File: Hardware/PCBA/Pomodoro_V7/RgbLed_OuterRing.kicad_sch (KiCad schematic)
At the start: 34 parts, among them J2 Conn_01x01_Pin

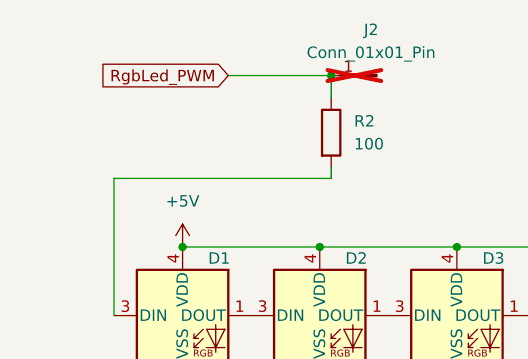
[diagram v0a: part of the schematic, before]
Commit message: Verified the microcontroller Pinout; Added basic peripheral wiring; Added the USBC Wiring
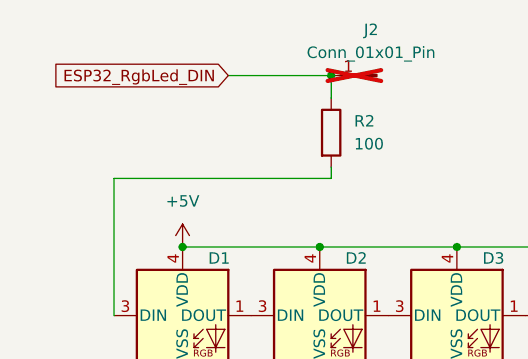
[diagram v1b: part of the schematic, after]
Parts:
- J2: now left out of the parts list
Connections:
- net RgbLed_PWM renamed ESP32_RgbLed_DIN
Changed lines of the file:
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@@
 		)
 	)
-	(global_label "RgbLed_PWM"
+	(global_label "ESP32_RgbLed_DIN"
 		(shape input)
 		(at 48.26 19.05 180)
@@
 		)
 		(property "Intersheetrefs" "${INTERSHEET_REFS}"
-			(at 33.3007 19.05 0)
+			(at 27.2531 19.05 0)
 			(effects
 				(font
@@
 		(unit 1)
 		(exclude_from_sim no)
-		(in_bom yes)
+		(in_bom no)
 		(on_board yes)
 		(dnp yes)

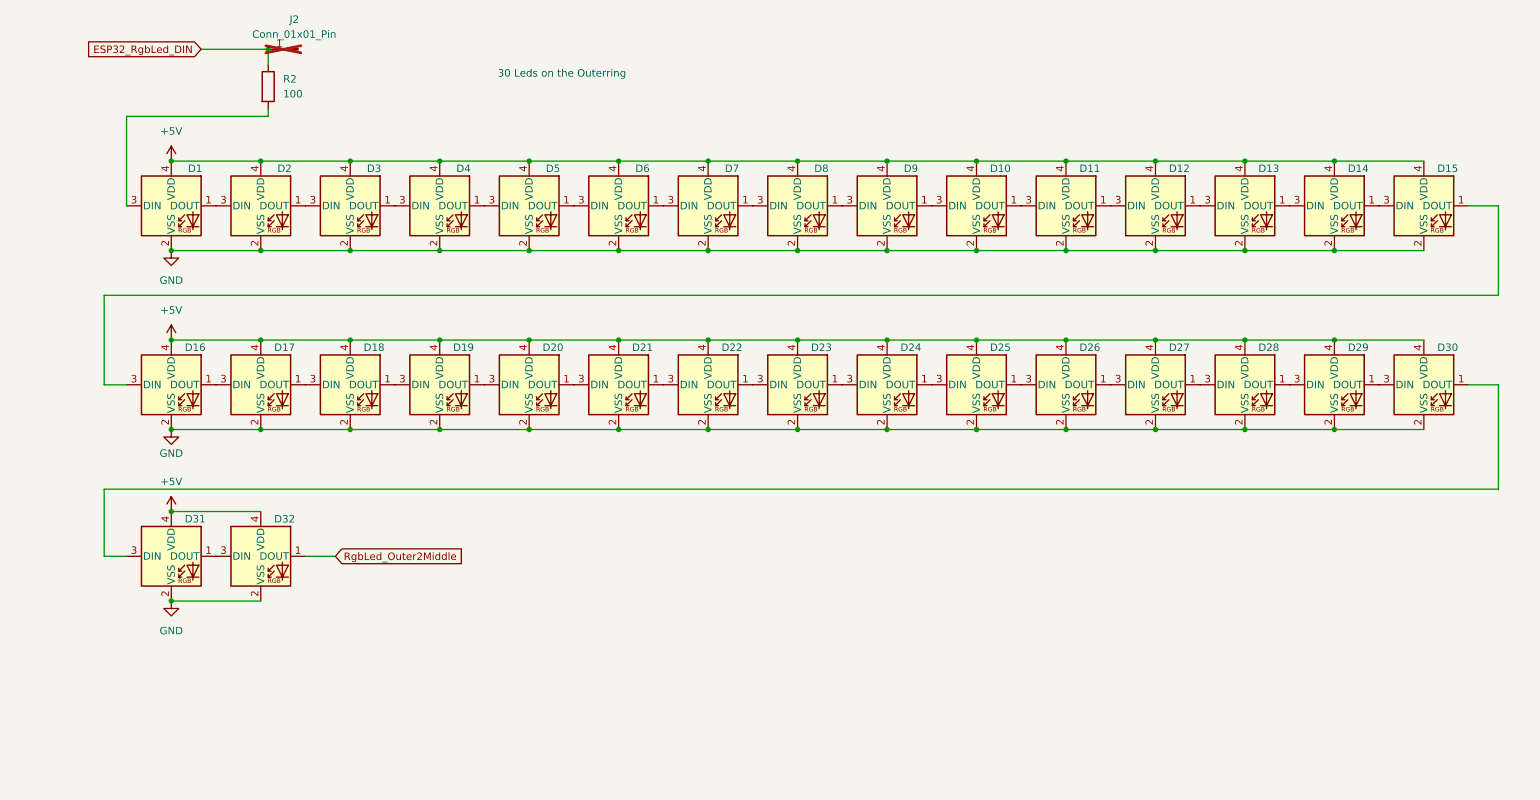
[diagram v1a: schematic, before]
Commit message: FW can now be flashed to an ESP32-S2 Target; Completed the Schematic
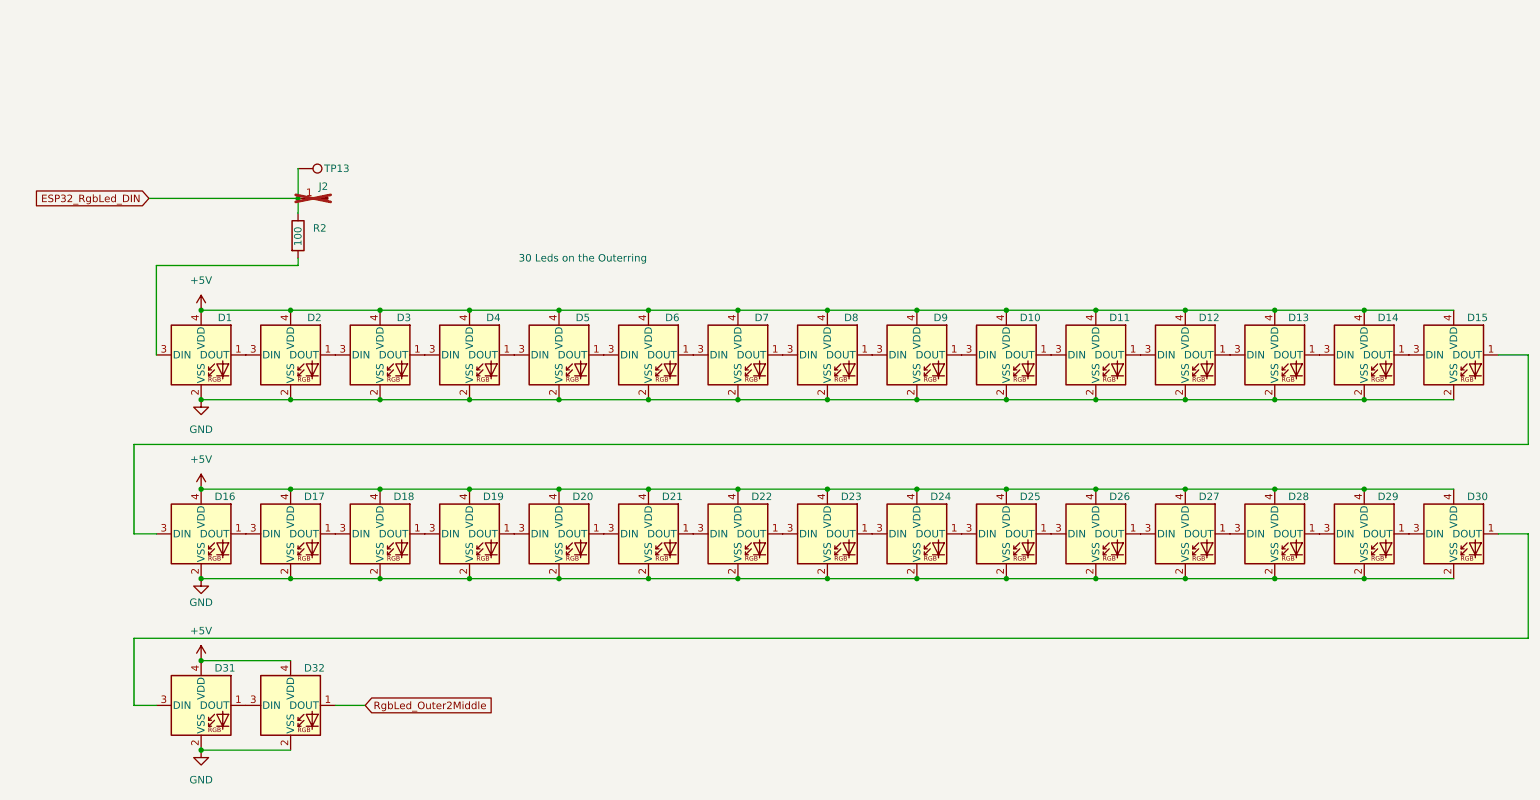
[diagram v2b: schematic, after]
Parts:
- added TP13: TestPoint, TestPoint:TestPoint_Pad_D1.0mm, symbol Connector:TestPoint
- J2: now in the parts list
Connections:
- net ESP32_RgbLed_DIN: now also TP13.1
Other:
- moved on the sheet: D1, D10, D11, D12, D13, D14, D15, D16, D17, D18, D19, D2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

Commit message: Update on the PCBA
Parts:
- renumbered J2 to J14, R2 to R11, TP13 to TP34
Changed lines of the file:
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@@
 		(dnp no)
 		(fields_autoplaced yes)
-		(property "Reference" "#PWR011"
+		(property "Reference" "#PWR051"
 			(at 48.26 97.79 0)
 			(effects
@@
 			(project "Pomodoro_V7"
 				(path "/7b50fc13-bee1-48b7-8eab-d6ef36855383/d366a572-4eed-4be8-88cc-5fb5da022e23/b6c0abfc-b228-4088-82f2-4b654b638967"
-					(reference "#PWR011")
+					(reference "#PWR051")
 					(unit 1)
 				)
@@
 		(on_board yes)
 		(dnp no)
-		(property "Reference" "R2"
+		(property "Reference" "R11"
 			(at 67.31 49.5299 0)
 			(effects
@@
 			(project "Pomodoro_V7"
 				(path "/7b50fc13-bee1-48b7-8eab-d6ef36855383/d366a572-4eed-4be8-88cc-5fb5da022e23/b6c0abfc-b228-4088-82f2-4b654b638967"
-					(reference "R2")
+					(reference "R11")
 					(unit 1)
 				)
@@
 		(on_board yes)
 		(dnp yes)
-		(property "Reference" "J2"
+		(property "Reference" "J14"
 			(at 69.088 42.418 0)
 			(effects
@@
 			(project "Pomodoro_V7"
 				(path "/7b50fc13-bee1-48b7-8eab-d6ef36855383/d366a572-4eed-4be8-88cc-5fb5da022e23/b6c0abfc-b228-4088-82f2-4b654b638967"
-					(reference "J2")
+					(reference "J14")
 					(unit 1)
 				)
@@
 		(dnp no)
 		(fields_autoplaced yes)
-		(property "Reference" "#PWR014"
+		(property "Reference" "#PWR054"
 			(at 48.26 144.78 0)
 			(effects
@@
 			(project "Pomodoro_V7"
 				(path "/7b50fc13-bee1-48b7-8eab-d6ef36855383/d366a572-4eed-4be8-88cc-5fb5da022e23/b6c0abfc-b228-4088-82f2-4b654b638967"
-					(reference "#PWR014")
+					(reference "#PWR054")
 					(unit 1)
 				)
@@
 		(dnp no)
 		(fields_autoplaced yes)
-		(property "Reference" "#PWR013"
+		(property "Reference" "#PWR053"
 			(at 48.26 127 0)
 			(effects
@@
 			(project "Pomodoro_V7"
 				(path "/7b50fc13-bee1-48b7-8eab-d6ef36855383/d366a572-4eed-4be8-88cc-5fb5da022e23/b6c0abfc-b228-4088-82f2-4b654b638967"
-					(reference "#PWR013")
+					(reference "#PWR053")
 					(unit 1)
 				)
@@
 		(dnp no)
 		(fields_autoplaced yes)
-		(property "Reference" "#PWR09"
+		(property "Reference" "#PWR049"
 			(at 48.26 67.31 0)
 			(effects
@@
 			(project "Pomodoro_V7"
 				(path "/7b50fc13-bee1-48b7-8eab-d6ef36855383/d366a572-4eed-4be8-88cc-5fb5da022e23/b6c0abfc-b228-4088-82f2-4b654b638967"
-					(reference "#PWR09")
+					(reference "#PWR049")
 					(unit 1)
 				)
@@
 		(on_board yes)
 		(dnp no)
-		(property "Reference" "TP13"
+		(property "Reference" "TP34"
 			(at 71.374 39.37 90)
 			(effects
@@
 			(project "Pomodoro_V7"
 				(path "/7b50fc13-bee1-48b7-8eab-d6ef36855383/d366a572-4eed-4be8-88cc-5fb5da022e23/b6c0abfc-b228-4088-82f2-4b654b638967"
-					(reference "TP13")
+					(reference "TP34")
 					(unit 1)
 				)
@@
 		(on_board yes)
 		(dnp no)
-		(property "Reference" "#PWR012"
+		(property "Reference" "#PWR052"
 			(at 48.26 115.57 0)
 			(effects
@@
 			(project "Pomodoro_V7"
 				(path "/7b50fc13-bee1-48b7-8eab-d6ef36855383/d366a572-4eed-4be8-88cc-5fb5da022e23/b6c0abfc-b228-4088-82f2-4b654b638967"
-					(reference "#PWR012")
+					(reference "#PWR052")
 					(unit 1)
 				)
@@
 		(dnp no)
 		(fields_autoplaced yes)
-		(property "Reference" "#PWR010"
+		(property "Reference" "#PWR050"
 			(at 48.26 85.09 0)
 			(effects
@@
 			(project "Pomodoro_V7"
 				(path "/7b50fc13-bee1-48b7-8eab-d6ef36855383/d366a572-4eed-4be8-88cc-5fb5da022e23/b6c0abfc-b228-4088-82f2-4b654b638967"
-					(reference "#PWR010")
+					(reference "#PWR050")
 					(unit 1)
 				)

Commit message: Updated the PCBA Files
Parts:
- R11: value 100 -> 100R(1%)
- TP34: now not fitted
